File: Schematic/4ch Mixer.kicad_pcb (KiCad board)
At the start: 2 copper layers, 45 x 100 mm, 49 parts, among them J1 3.5mm_Mono_Jack_With_Switch, J2 3.5mm_Mono_Jack_With_Switch, J3 3.5mm_Mono_Jack_With_Switch, J4 3.5mm_Mono_Jack_With_Switch, J5 3.5mm_Mono_Jack_With_Switch, J6 3.5mm_Mono_Jack_With_Switch, P1 CONN_02X08, U1 TL074, U2 TL072

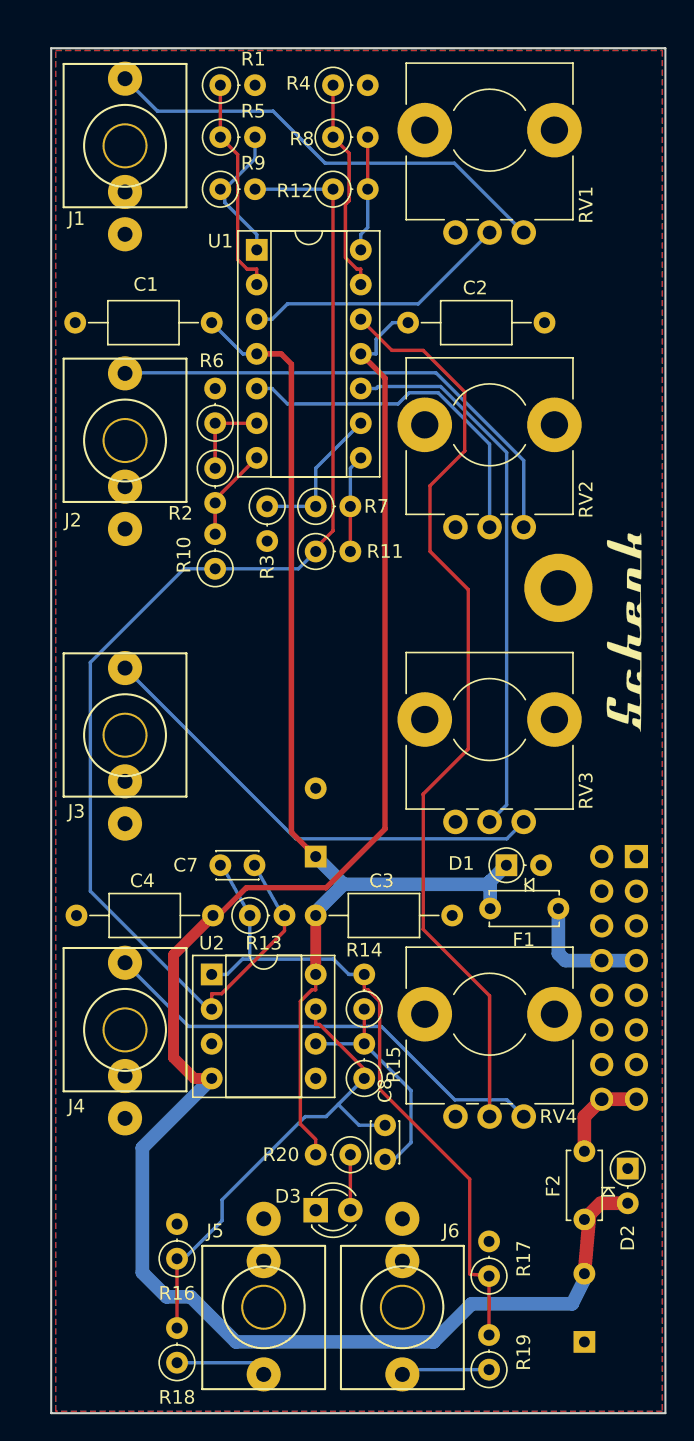
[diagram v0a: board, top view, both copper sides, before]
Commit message: Generate SMD board placement from netlist
tools/pcb: netlist-driven board generator and the 4ch mixer layout.
Input jacks in a column beside their pots, pots 26 mm apart along the
full 100 mm length, outputs on the right near the bottom. No routing yet.
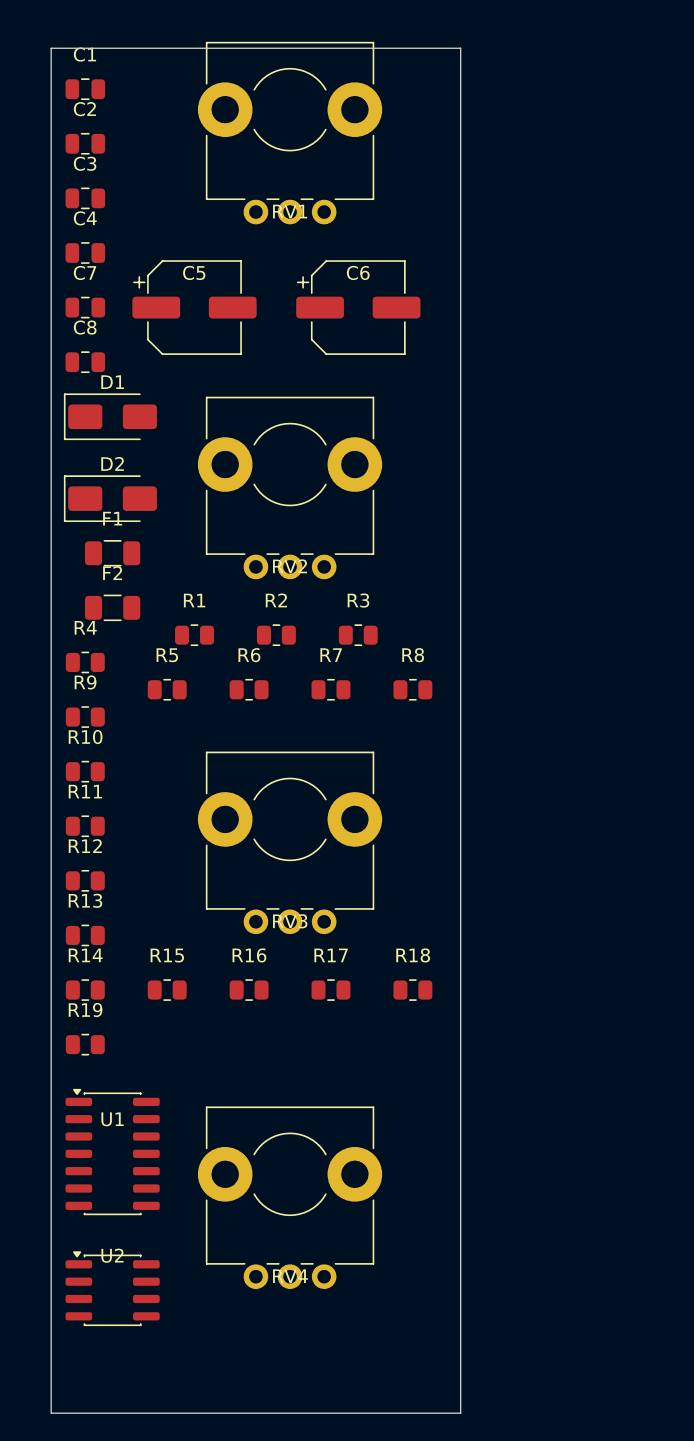
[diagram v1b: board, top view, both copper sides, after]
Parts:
- removed D3: LED, LED_THT:LED_D3.0mm
- removed G*** (x2): LOGO, _NTSFootprints:SchenkLogo
- removed J1, J2, J3, J4, J5, J6: 3.5mm_Mono_Jack_With_Switch, _NTSFootprints:3.5mm_Mono_Vertical_QuingPu_WQP-PJ301M-12
- removed P1: CONN_02X08, Connector_PinHeader_2.54mm:PinHeader_2x08_P2.54mm_Vertical
- removed R20: 1k, Resistor_THT:R_Axial_DIN0207_L6.3mm_D2.5mm_P2.54mm_Vertical
- removed REF**: 2.5mmMountingHole, _NTSFootprints:2.5mmMountingHole
- C1, C2, C3, C4: footprint Capacitor_THT:C_Axial_L5.1mm_D3.1mm_P10.00mm_Horizontal -> C_0805_2012Metric
- C5, C6: footprint Capacitor_THT:CP_Radial_D8.0mm_P5.00mm -> CP_Elec_6.3x5.4; moved to F.Cu
- C7, C8: footprint Capacitor_THT:C_Disc_D3.0mm_W2.0mm_P2.50mm -> C_0805_2012Metric
- D1, D2: footprint Diode_THT:D_DO-35_SOD27_P2.54mm_Vertical_AnodeUp -> D_SMA
- F1, F2: footprint Capacitor_THT:C_Disc_D5.0mm_W2.5mm_P5.00mm -> Fuse_1206_3216Metric
- R1, R10, R11, R12, R13, R14, R15, R16, R17, R18, R19, R2, R3, R4, R5, R6, R7, R8, R9: footprint Resistor_THT:R_Axial_DIN0207_L6.3mm_D2.5mm_P2.54mm_Vertical -> R_0805_2012Metric
- RV1, RV2, RV3, RV4: footprint Potentiometer_THT:Potentiometer_Alps_RK09L_Single_Horizontal -> Potentiometer_Alps_RK09L_Plated_Mount_Holes
- U1: footprint Package_DIP:DIP-14_W7.62mm_Socket -> SOIC-14_3.9x8.7mm_P1.27mm
- U2: footprint Package_DIP:DIP-8_W7.62mm_Socket -> SOIC-8_3.9x4.9mm_P1.27mm
- moved C6 77.6 mm to (122.5, 69.0), turned to 0 degrees
- moved U1 67.1 mm to (104.5, 131.0)
- moved D2 61.9 mm to (104.5, 83.0), turned to 0 degrees
- moved C8 60.1 mm to (102.5, 73.0), turned to 0 degrees
- moved C3 55.2 mm to (102.5, 61.0)
- moved R12 53.8 mm to (102.5, 111.0)
- moved F2 52.7 mm to (104.5, 91.0), turned to 0 degrees
- moved C4 48.5 mm to (102.5, 65.0)
- moved R4 46.0 mm to (102.5, 95.0)
- moved D1 43.7 mm to (104.5, 77.0)
- moved C7 42.0 mm to (102.5, 69.0)
- moved F1 41.8 mm to (104.5, 87.0), turned to 0 degrees
- moved C5 41.2 mm to (110.5, 69.0), turned to 0 degrees
- moved R8 40.9 mm to (126.5, 97.0)
- moved R5 40.7 mm to (108.5, 97.0)
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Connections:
- C1 pad 1: +12VA -> Net-(D1-K)
- C1 pad 2: GNDA -> Net-(C1-~-Pad2)
- C2 pad 1: GNDA -> Net-(C1-~-Pad2)
- C3 pad 2: GNDA -> Net-(C3-~-Pad2)
- C4 pad 1: GNDA -> Net-(C3-~-Pad2)
- C5 pad 1: +12VA -> Net-(D1-K)
- C5 pad 2: GNDA -> Net-(C5-~-Pad2)
- C6 pad 1: GNDA -> Net-(C5-~-Pad2)
- C7 pad 2: Net-(C7-Pad2) -> Net-(U2A--)
- D1 pad 1: +12VA -> Net-(D1-K)
- D1 pad 2: GNDA -> Net-(D1-A)
- D2 pad 1: GNDA -> Net-(D1-A)
- F1 pad 2: +12VA -> Net-(D1-K)
- R10 pad 1: Net-(C7-Pad2) -> Net-(R10-~-Pad1)
- R11 pad 1: Net-(C7-Pad2) -> Net-(R11-~-Pad1)
- R12 pad 1: Net-(C7-Pad2) -> Net-(R10-~-Pad1)
- R13 pad 2: Net-(C7-Pad2) -> Net-(R11-~-Pad1)
- R9 pad 2: Net-(C7-Pad2) -> Net-(R10-~-Pad1)
- U2 pad 2: Net-(C7-Pad2) -> Net-(U2A--)
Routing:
- net -12VA: track 132.3 -> 0.00 mm
- net Net-(C7-Pad2): track 96.5 -> 0.00 mm
- net +12VA: track 83.6 -> 0.00 mm
- net Net-(U1D-+): track 68.5 -> 0.00 mm
- net Net-(U2A-~): track 50.6 -> 0.00 mm
- net Net-(U1C-+): track 40.3 -> 0.00 mm
- net Net-(J2-PadT): track 36.8 -> 0.00 mm
- net Net-(U2B-~): track 36.3 -> 0.00 mm
- net Net-(J3-PadT): track 34.9 -> 0.00 mm
- net Net-(J4-PadT): track 33.9 -> 0.00 mm
- net Net-(J1-PadT): track 33.9 -> 0.00 mm
- net Net-(U1B-+): track 25.5 -> 0.00 mm
- net Net-(U1A-+): track 19.7 -> 0.00 mm
- net Net-(U2B--): track 17.2 -> 0.00 mm
- net Net-(U1A--): track 16.1 -> 0.00 mm
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- removed copper zone on B.Cu, net GNDA
- removed copper zone on F.Cu, net GNDA
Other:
- board size 45 x 100 mm -> 30 x 100 mm
- board text removed: "+12V"
- board text removed: "-12V"
- board text removed: "4ch Summing Amp v1.0"
- board text removed: "GND"

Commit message: Place 4ch mixer board: pots right, inputs left, outputs in pot gaps
Pots RV1-RV4 on the right at 24 mm pitch, input jacks J1-J4 beside their
pots on the left, outputs J5/J6 in the gaps between pots 2-4, header P1 on
the bottom edge. SMD parts are mirrored onto the back, packed around the
through-hole parts. DRC: only the jack footprint's hole/mask clearance
warnings remain (the Attenuverter has the same ones). No routing yet.
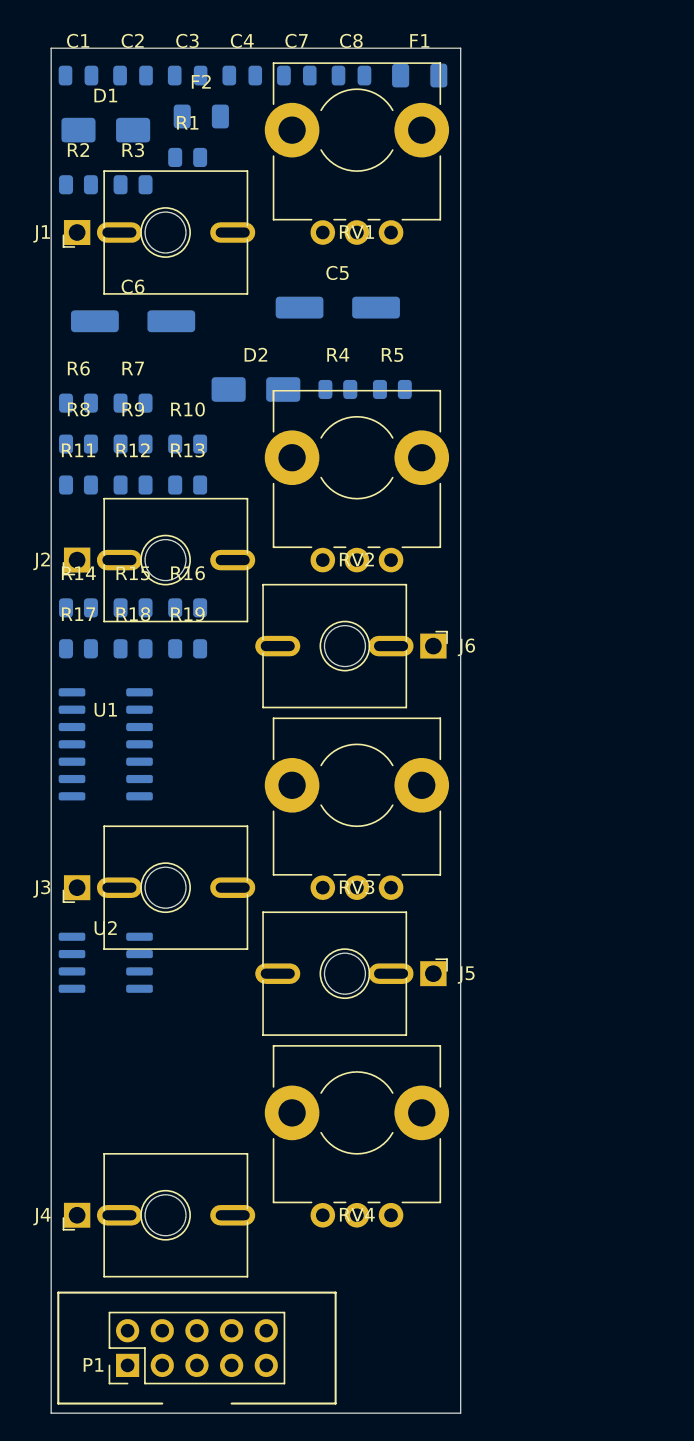
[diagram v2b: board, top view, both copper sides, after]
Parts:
- added J1: ~, Jack_3.5mm_QingPu_WQP-PJ398SM_Vertical_CenterHole_OvalPads, F.Cu at (101.9, 63.5)
- added J2: ~, Jack_3.5mm_QingPu_WQP-PJ398SM_Vertical_CenterHole_OvalPads, F.Cu at (101.9, 87.5)
- added J3: ~, Jack_3.5mm_QingPu_WQP-PJ398SM_Vertical_CenterHole_OvalPads, F.Cu at (101.9, 111.5)
- added J4: ~, Jack_3.5mm_QingPu_WQP-PJ398SM_Vertical_CenterHole_OvalPads, F.Cu at (101.9, 135.5)
- added J5: ~, Jack_3.5mm_QingPu_WQP-PJ398SM_Vertical_CenterHole_OvalPads, F.Cu at (128.0, 117.8)
- added J6: ~, Jack_3.5mm_QingPu_WQP-PJ398SM_Vertical_CenterHole_OvalPads, F.Cu at (128.0, 93.8)
- added P1: Power, PinHeader_2x05_P2.54mm_Vertical_Shrouded, F.Cu at (105.6, 146.5)
- C1, C2, C3, C4, C5, C6, C7, C8, D1, D2, F1, F2, R1, R10, R11, R12, R13, R14, R15, R16, R17, R18, R19, R2, R3, R4, R5, R6, R7, R8, R9, U1, U2: moved to B.Cu
- moved F1 41.6 mm to (127.0, 52.0)
- moved R3 36.9 mm to (106.0, 60.0)
- moved F2 36.6 mm to (111.0, 55.0)
- moved R2 36.0 mm to (102.0, 60.0)
- moved R1 35.0 mm to (110.0, 58.0)
- moved R13 33.8 mm to (110.0, 82.0)
- moved R18 32.3 mm to (106.0, 94.0)
- moved R17 31.1 mm to (102.0, 94.0)
- moved R8 30.4 mm to (102.0, 79.0)
- moved U1 30.0 mm to (104.0, 101.0)
- moved R19 30.0 mm to (110.0, 94.0)
- moved R12 29.2 mm to (106.0, 82.0)
- moved C8 28.7 mm to (122.0, 52.0)
- moved R16 28.4 mm to (110.0, 91.0)
- moved R15 28.1 mm to (106.0, 91.0)
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
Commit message: Board placement for hand tuning (DRC errors remain)
Header P1 on the back at the top left, outputs J5/J6 in the lower right,
pots 24 mm apart. Remaining DRC errors are listed for manual placement
fixes. Not routed.
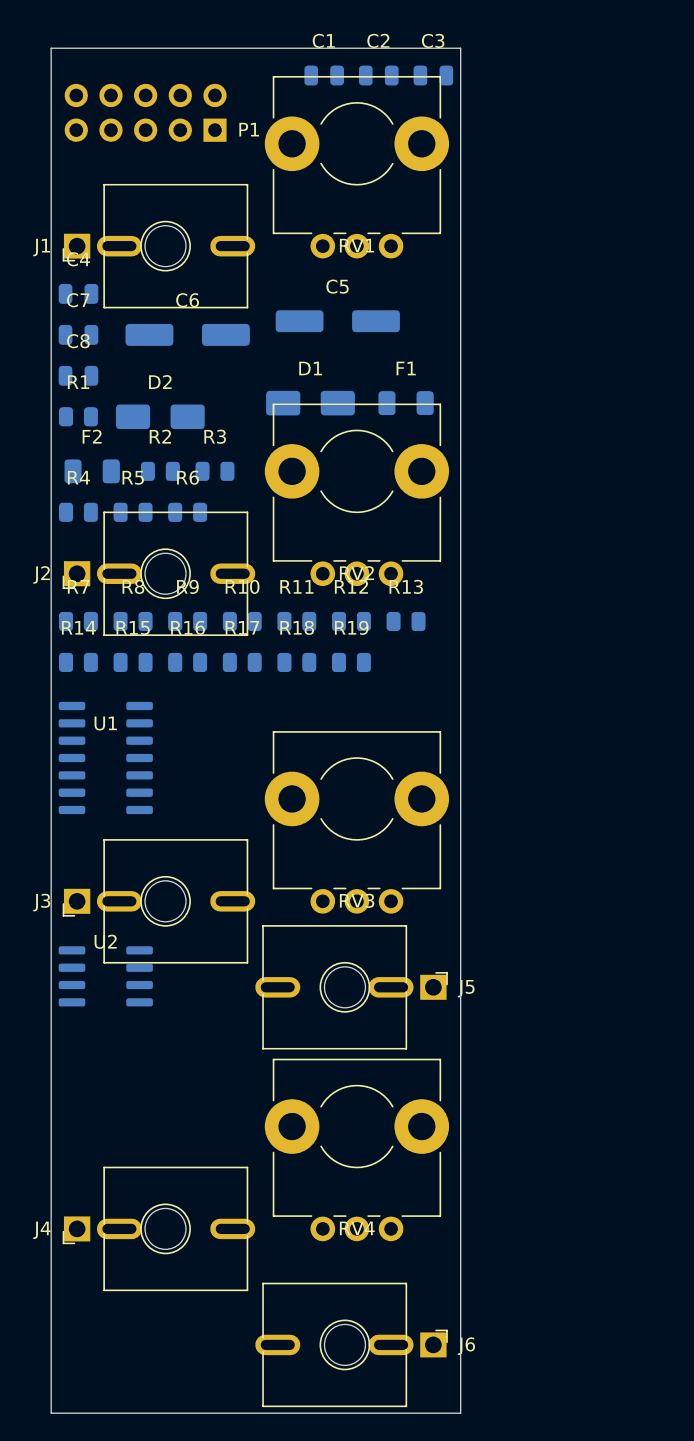
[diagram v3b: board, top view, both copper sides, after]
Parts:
- P1: moved to B.Cu
- moved P1 90.7 mm to (112.0, 56.0), turned to 270 degrees
- moved J6 51.2 mm to (128.0, 145.0)
- moved C8 29.7 mm to (102.0, 74.0)
- moved F2 27.2 mm to (103.0, 81.0)
- moved D1 25.0 mm to (119.0, 76.0)
- moved C7 24.8 mm to (102.0, 71.0)
- moved F1 24.0 mm to (126.0, 76.0)
- moved R2 21.8 mm to (108.0, 81.0)
- moved R3 21.8 mm to (112.0, 81.0)
- moved R4 21.0 mm to (102.0, 84.0)
- moved R5 21.0 mm to (106.0, 84.0)
- moved R1 20.6 mm to (102.0, 77.0)
- moved C4 20.0 mm to (102.0, 68.0)
- moved R11 18.9 mm to (118.0, 92.0)
- moved R12 18.9 mm to (122.0, 92.0)
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
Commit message: Use the Attenuverter's jack footprint orientation
The newer NTS jack footprint defines its pads at 180 degrees; the
Attenuverter board uses 270, so the oval holes were 90 degrees off. Replace
the project copy with the Attenuverter's version. Also stop writing a
second UUID on each pad in the generator. Board regenerated: only the
pot 1 / header courtyard clash remains.
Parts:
- moved R1 27.5 mm to (128.0, 68.0)
- moved R13 24.2 mm to (102.0, 95.0)
- moved F1 23.3 mm to (103.0, 80.0)
- moved R2 22.4 mm to (128.0, 71.0)
- moved D2 15.0 mm to (123.0, 76.0)
- moved R6 11.3 mm to (102.0, 92.0)
- moved R3 10.2 mm to (102.0, 83.0)
- moved C8 10.0 mm to (110.0, 68.0)
- moved F2 6.08 mm to (109.0, 80.0)
- moved C6 5.00 mm to (106.0, 74.0)
- moved C7 5.00 mm to (106.0, 68.0)
- moved R4 4.12 mm to (106.0, 83.0)
- moved R5 4.12 mm to (110.0, 83.0)
- moved D1 4.00 mm to (115.0, 76.0)
- moved R10 4.00 mm to (118.0, 92.0)
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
